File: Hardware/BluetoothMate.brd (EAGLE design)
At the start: 44.5 x 16.5 mm, 26 parts, among them Q1 MOSFET-NCHANNELSMD, Q2 MOSFET-NCHANNELSMD, U1 BLUETOOTH-RN41, U3 V_REG_LDOSMD

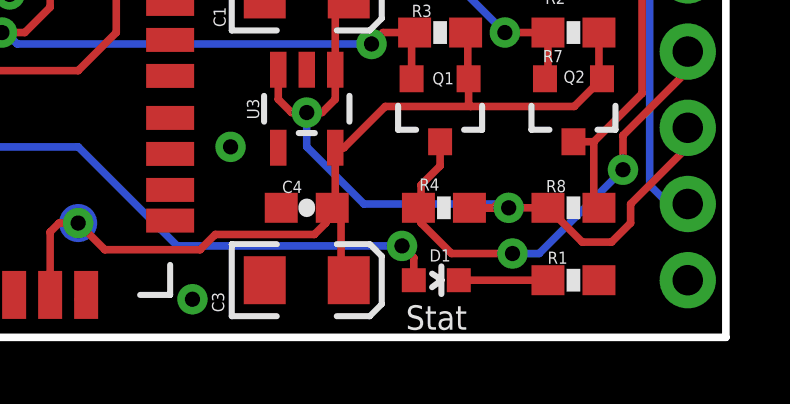
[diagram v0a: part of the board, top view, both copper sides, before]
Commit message: Fix silk screen/symbol errors
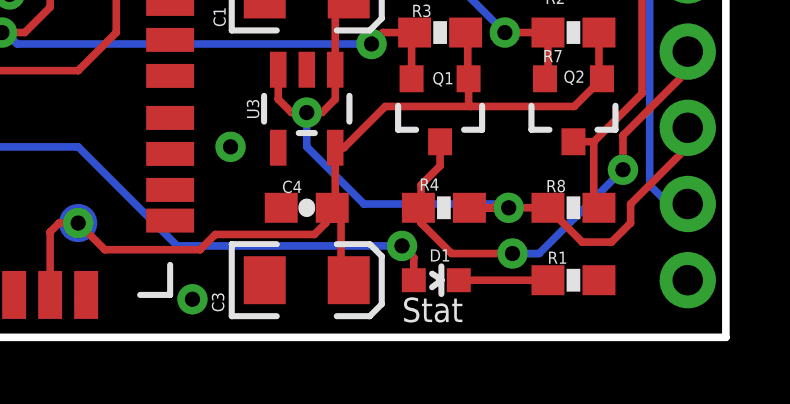
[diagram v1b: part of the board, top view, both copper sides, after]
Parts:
- added U$2: REVISION, SparkFun-Aesthetics:REVISION
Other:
- board text added: "J. Lindblom"
- board text added: "T. Klopfenstein"
- board text removed: "J. Lindblom, T. Klopfenstein"

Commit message: Added 2nd fiducial
Production files updated to v16a
Hardware files updated also
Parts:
- added JP4: FIDUCIAL1X2.5, abes:FIDUCIAL-1X2.5
